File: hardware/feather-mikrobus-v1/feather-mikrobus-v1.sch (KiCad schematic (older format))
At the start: 26 parts, among them J1 Adafruit_Feather_socket_heade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, J2 Adafruit_Feather_socket_heade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, J3 mikroBUS_socket_header_left_p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, J4 mikroBUS_socket_header_right_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, SW1 JS102011SAQN, SW2 KMR421GULCLFS, SW3 KMR421GULCLFS

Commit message: Update symbols and minor cleanup
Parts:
- removed A1: Adafruit_Feather_socket_empty, Flying_Camp_Design:Adafruit_Feather_socket_empty, symbol Flying_Camp_Design:Adafruit_Feather_socket_empty
- removed A2: mikroBUS_socket_empty, Flying_Camp_Design:mikroBUS_socket_empty, symbol Flying_Camp_Design:mikroBUS_socket_empty
- C1: value GRM188R72A104KA35D -> Murata_GRM188R72A104KA35D; symbol Flying_Camp_Design:GRM188R72A104KA35D -> Flying_Camp_Design:Murata_GRM188R72A104KA35D
- D1, D2: value LTST-C191KGKT -> Lite-On_LTST-C191KGKT; symbol Flying_Camp_Design:LTST-C191KGKT -> Flying_Camp_Design:Lite-On_LTST-C191KGKT
- LOGO1: value mikroBUS_logo -> mikroBUS-Logo_11.9x4.1mm_SilkScreen; symbol Flying_Camp_Design:mikroBUS_logo -> Flying_Camp_Design:mikroBUS-Logo_11.9x4.1mm_SilkScreen
- LOGO3: value Adafruit_Feather_logo -> Adafruit_Feather_logo_13.87x6.33mm_silkscreen; footprint Flying_Camp_Design:Adafruit_Feather_logo -> Flying_Camp_Design:Adafruit_Feather_logo_13.87x6.33mm_silkscreen; symbol Flying_Camp_Design:Adafruit_Feather_logo -> Flying_Camp_Design:Adafruit_Feather_logo_13.87x6.33mm_silkscreen
- R1: value RC0603JR-071KL -> Yageo_RC0603JR-071KL; symbol Flying_Camp_Design:RC0603JR-071KL -> Flying_Camp_Design:Yageo_RC0603JR-071KL
- R2, R8: value RC0603JR-07330RL -> Yageo_RC0603JR-07330RL; symbol Flying_Camp_Design:RC0603JR-07330RL -> Flying_Camp_Design:Yageo_RC0603JR-07330RL
- R3, R4: value RC0603JR-074K7L -> Yageo_RC0603JR-074K7L; symbol Flying_Camp_Design:RC0603JR-074K7L -> Flying_Camp_Design:Yageo_RC0603JR-074K7L; DNP (none) -> DNP
- R5: value RC0603JR-070RL -> Yageo_RC0603JR-070RL; symbol Flying_Camp_Design:RC0603JR-070RL -> Flying_Camp_Design:Yageo_RC0603JR-070RL
- R6: value RC0603JR-0710KL -> Yageo_RC0603JR-0710KL; symbol Flying_Camp_Design:RC0603JR-0710KL -> Flying_Camp_Design:Yageo_RC0603JR-0710KL
- R7: value RC0603JR-07100RL -> Yageo_RC0603JR-07100RL; symbol Flying_Camp_Design:RC0603JR-07100RL -> Flying_Camp_Design:Yageo_RC0603JR-07100RL
- SW1: value JS102011SAQN -> C_and_K_JS102011SAQN; footprint Flying_Camp_Design:JS102011SAQN -> Flying_Camp_Design:C_and_K_JS102011SAQN; symbol Flying_Camp_Design:JS102011SAQN -> Flying_Camp_Design:C_and_K_JS102011SAQN
- SW2, SW3: value KMR421GULCLFS -> C_and_K_KMR421GULCLFS; footprint Flying_Camp_Design:KMR421GULCLFS -> Flying_Camp_Design:C_and_K_KMR421GULCLFS; symbol Flying_Camp_Design:KMR421GULCLFS -> Flying_Camp_Design:C_and_K_KMR421GULCLFS
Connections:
- net labels added: 3V3_LED_R, EN_SW_R, SW2_R, USER_LED_R, ~USER_SW
- net labels removed: USER_SW
- wire segments 106 -> 107
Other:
- note added: "Adafruit STM32F405 Feather Express Notes:\n- No PWM output on D6-D8\n- DAC output available on A0-A1\n- D8 is connected to onboard LED"
- note removed: "Adafruit STM32F405 Feather Express Notes:\n- No PWM output on D6-D8\n- DAC output on A0-A1\n- D8 is connected to onboard LED"
- moved on the sheet: FID1, FID2, FID3, J1, J2, J3, J4

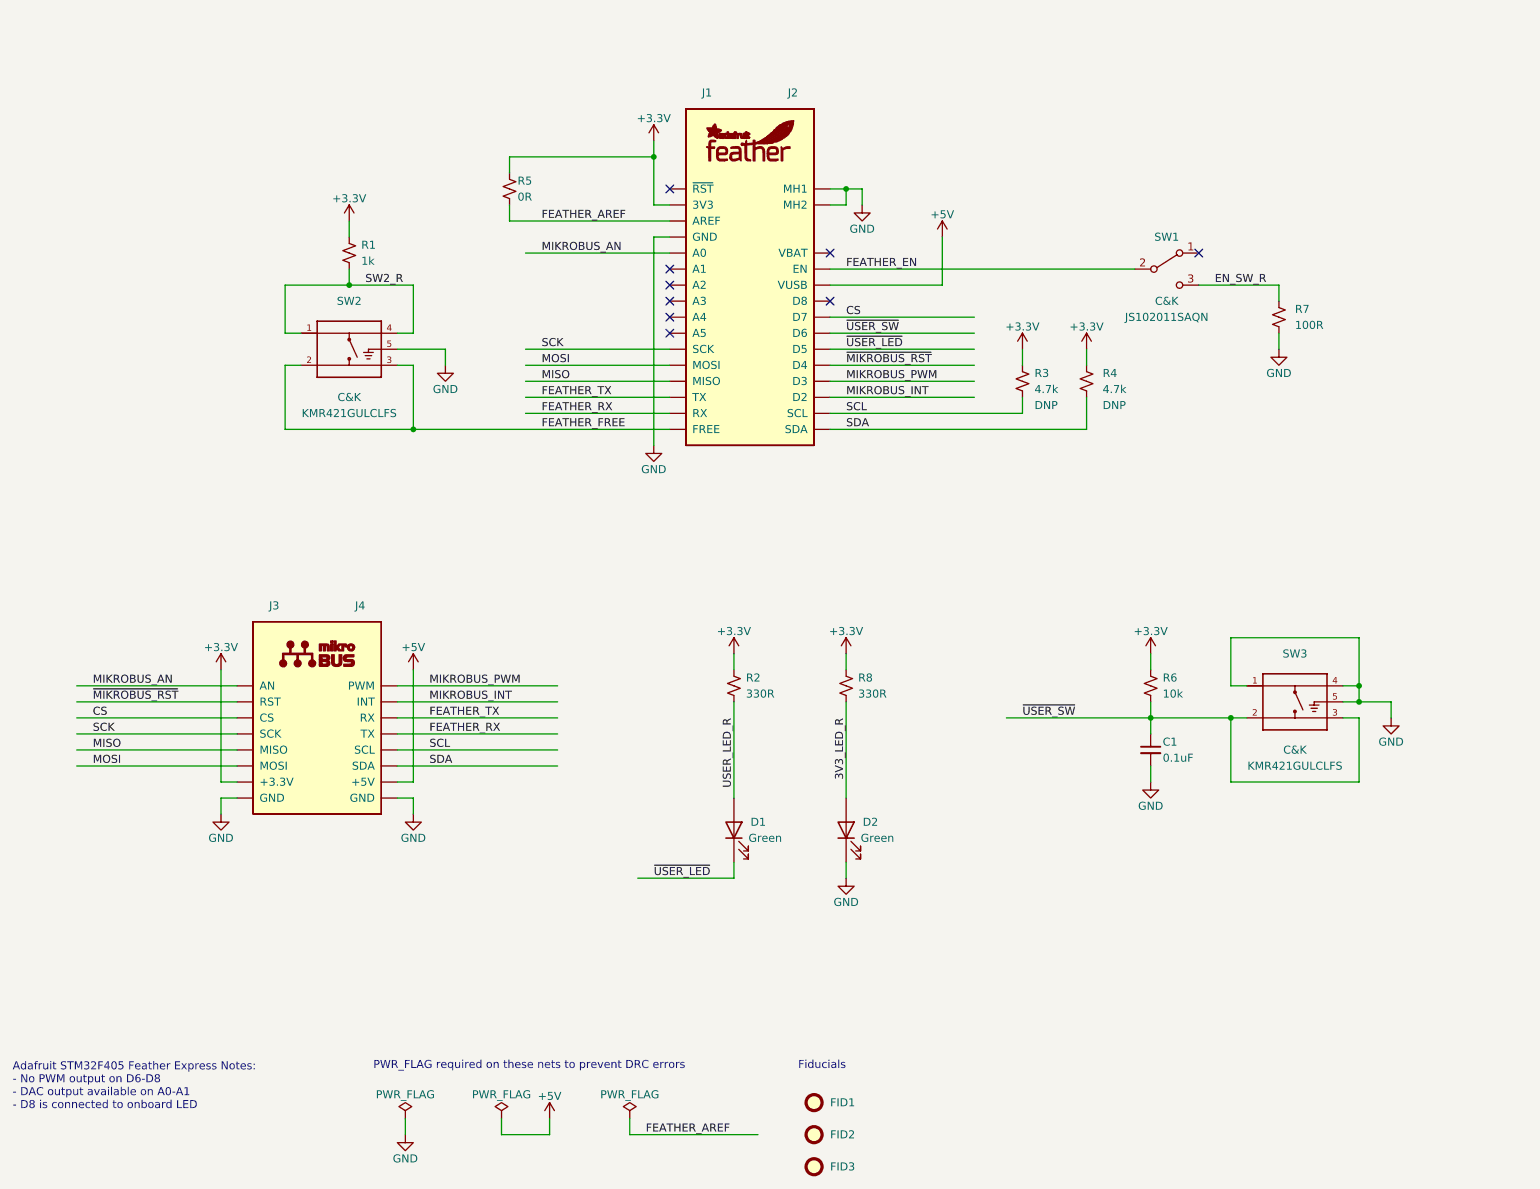
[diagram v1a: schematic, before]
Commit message: Update schematic with finalized manufacturers and vendors
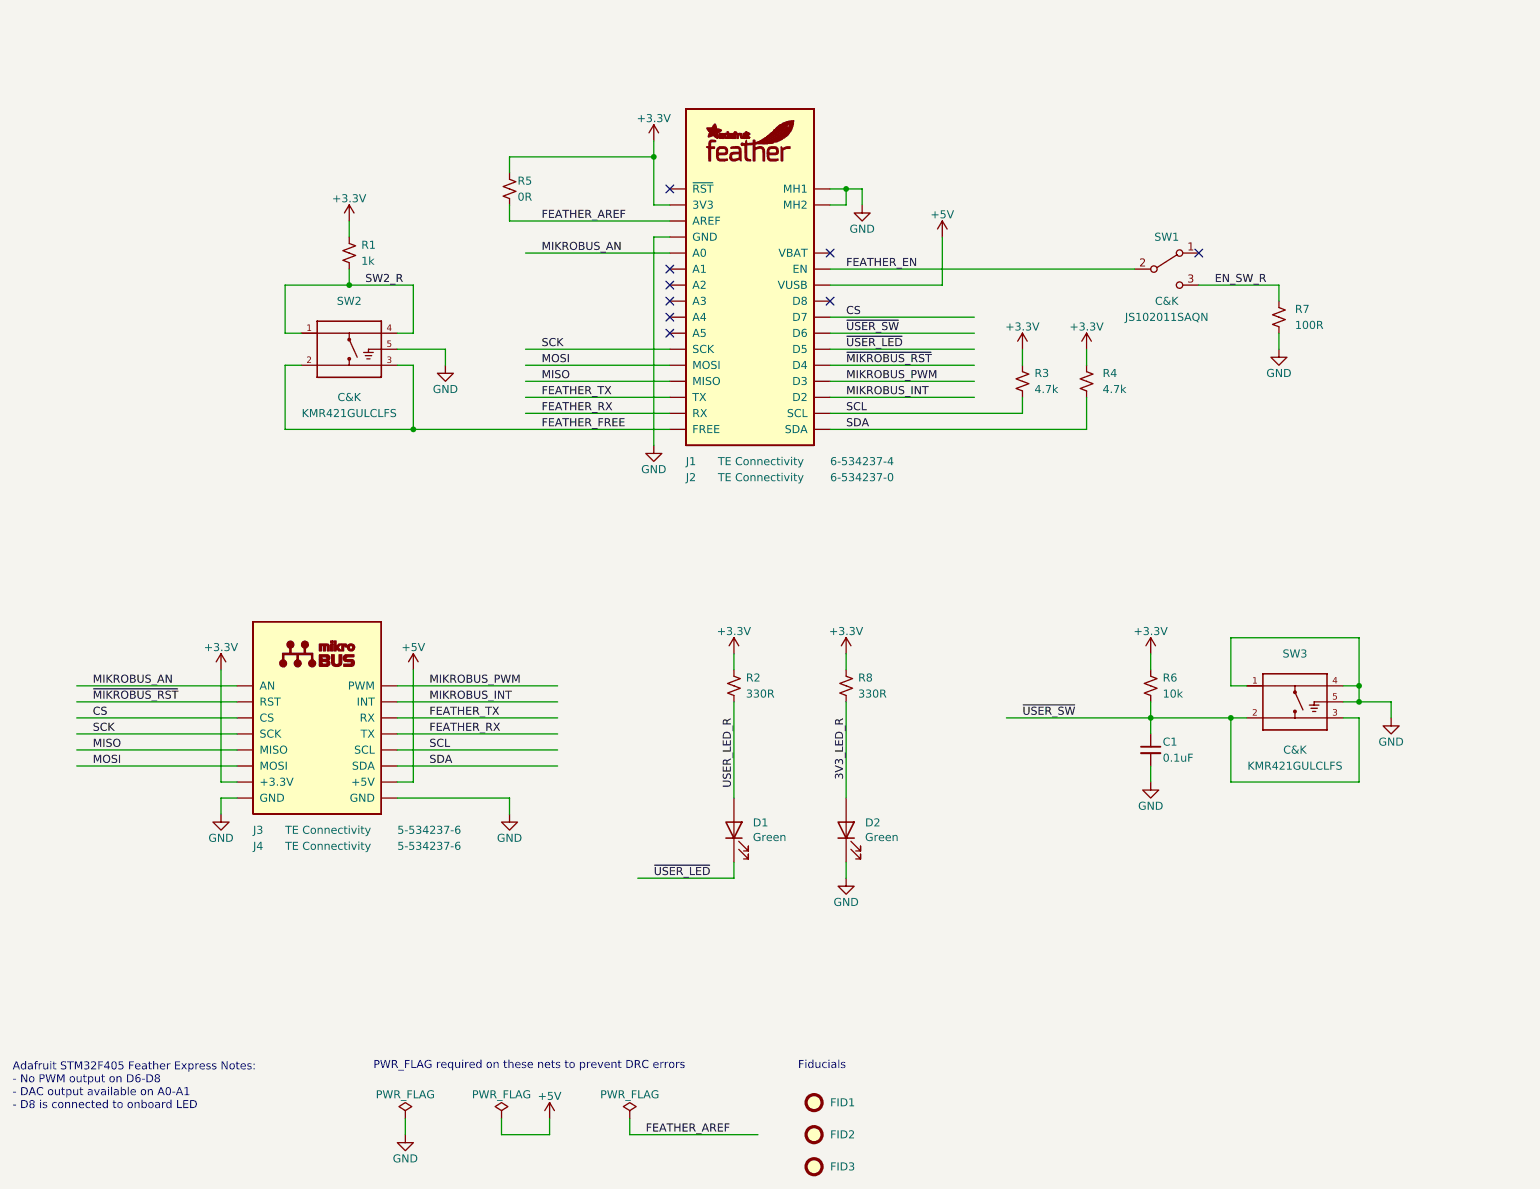
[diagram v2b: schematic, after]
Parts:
- removed D1, D2: Lite-On_LTST-C191KGKT, Flying_Camp_Design:LED_0603_1608Metric, symbol Flying_Camp_Design:Lite-On_LTST-C191KGKT
- added D1, D2: Lite-On_LTST-C193KGKT-5A, Flying_Camp_Design:LED_0603_1608Metric, symbol Flying_Camp_Design:Lite-On_LTST-C193KGKT-5A
- J1: Manufacturer (none) -> TE Connectivity; Manufacturer Part Number (none) -> 6-534237-4; Vendor (none) -> Digi-Key; Vendor Part Number (none) -> A32549-ND; Vendor URL (none) -> https://www.digikey.com/short/z8mb48
- J2: Manufacturer (none) -> TE Connectivity; Manufacturer Part Number (none) -> 6-534237-0; Vendor (none) -> Digi-Key; Vendor Part Number (none) -> A32911-ND; Vendor URL (none) -> https://www.digikey.com/short/z8mbmc
- J3, J4: Manufacturer (none) -> TE Connectivity; Manufacturer Part Number (none) -> 5-534237-6; Vendor (none) -> Digi-Key; Vendor Part Number (none) -> A32909-ND; Vendor URL (none) -> https://www.digikey.com/short/z8mbmb
- R3, R4: DNP DNP -> (none)
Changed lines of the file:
@@
 CS
 Wire Wire Line
-	3300 5400 3300 5500
-Wire Wire Line
-	3200 5400 3300 5400
+	3900 5400 3900 5500
+Wire Wire Line
+	3200 5400 3900 5400
 Wire Wire Line
 	2200 4700 1200 4700
@@
 F 8 "https://www.digikey.com/short/z3bjcp" H 7600 1900 50  0001 L CNN "Vendor URL"
 F 9 "4.7k" H 7600 2750 50  0000 L CNN "Resistance"
-F 10 "DNP" H 7600 2650 50  0000 L CNN "DNP"
 	1    7500 2800
 	1    0    0    -1
@@
 F 8 "https://www.digikey.com/short/z3bjcp" H 7200 1900 50  0001 L CNN "Vendor URL"
 F 9 "4.7k" H 7175 2750 50  0000 L CNN "Resistance"
-F 10 "DNP" H 7175 2650 50  0000 L CNN "DNP"
 	1    7100 2800
 	1    0    0    -1
@@
 U 1 1 5E3B727D
 P 5400 2200
-F 0 "J1" H 5100 3400 50  0000 L CNN
+F 0 "J1" H 5000 1100 50  0000 L CNN
 F 1 "Adafruit_Feather_socket_header_left_pth" H 5400 900 50  0001 C CNN
 F 2 "Flying_Camp_Design:Adafruit_Feather_socket_header_left_pth" H 5400 800 50  0001 C CNN
-F 3 "https://learn.adafruit.com/adafruit-feather/feather-specification" H 5400 700 50  0001 C CNN
+F 3 "https://www.te.com/commerce/DocumentDelivery/DDEController?Action=srchrtrv&DocNm=534237&DocType=Customer+Drawing&DocLang=English" H 5400 700 50  0001 C CNN
+F 4 "TE Connectivity" H 5200 1100 50  0000 L CNN "Manufacturer"
+F 5 "6-534237-4" H 5900 1100 50  0000 L CNN "Manufacturer Part Number"
+F 6 "Digi-Key" H 0   0   50  0001 C CNN "Vendor"
+F 7 "A32549-ND" H 0   0   50  0001 C CNN "Vendor Part Number"
+F 8 "https://www.digikey.com/short/z8mb48" H 0   0   50  0001 C CNN "Vendor URL"
 	1    5400 2200
 	1    0    0    -1
@@
 U 1 1 5E3B67CD
 P 5400 2200
-F 0 "J2" H 5700 3400 50  0000 R CNN
+F 0 "J2" H 5000 1000 50  0000 L CNN
 F 1 "Adafruit_Feather_socket_header_right_pth" H 5400 900 50  0001 C CNN
 F 2 "Flying_Camp_Design:Adafruit_Feather_socket_header_right_pth" H 5400 800 50  0001 C CNN
-F 3 "https://learn.adafruit.com/adafruit-feather/feather-specification" H 5400 700 50  0001 C CNN
+F 3 "https://www.te.com/commerce/DocumentDelivery/DDEController?Action=srchrtrv&DocNm=534237&DocType=Customer+Drawing&DocLang=English" H 5400 700 50  0001 C CNN
+F 4 "TE Connectivity" H 5200 1000 50  0000 L CNN "Manufacturer"
+F 5 "6-534237-0" H 5900 1000 50  0000 L CNN "Manufacturer Part Number"
+F 6 "Digi-Key" H 0   0   50  0001 C CNN "Vendor"
+F 7 "A32911-ND" H 0   0   50  0001 C CNN "Vendor Part Number"
+F 8 "https://www.digikey.com/short/z8mbmc" H 0   0   50  0001 C CNN "Vendor URL"
 	1    5400 2200
 	1    0    0    -1
@@
 L Flying_Camp_Design:GND #PWR012
 U 1 1 5E3D743E
-P 3300 5500
-F 0 "#PWR012" H 3300 5250 50  0001 C CNN
-F 1 "GND" H 3300 5350 50  0000 C CNN
-F 2 "" H 3300 5500 50  0001 C CNN
-F 3 "" H 3300 5500 50  0001 C CNN
-	1    3300 5500
+P 3900 5500
+F 0 "#PWR012" H 3900 5250 50  0001 C CNN
+F 1 "GND" H 3900 5350 50  0000 C CNN
+F 2 "" H 3900 5500 50  0001 C CNN
+F 3 "" H 3900 5500 50  0001 C CNN
+	1    3900 5500
 	1    0    0    -1
 $EndComp
@@
 U 1 1 5E3C6EE3
 P 2700 4900
-F 0 "J3" H 2400 5600 50  0000 L CNN
+F 0 "J3" H 2300 4200 50  0000 L CNN
 F 1 "mikroBUS_socket_header_left_pth" H 2700 4000 50  0001 C CNN
 F 2 "Flying_Camp_Design:mikroBUS_socket_header_left_pth" H 2700 3900 50  0001 C CNN
-F 3 "https://www.mikroe.com/mikrobus" H 2700 3800 50  0001 C CNN
+F 3 "https://www.te.com/commerce/DocumentDelivery/DDEController?Action=srchrtrv&DocNm=534237&DocType=Customer+Drawing&DocLang=English" H 2700 3800 50  0001 C CNN
+F 4 "TE Connectivity" H 2500 4200 50  0000 L CNN "Manufacturer"
+F 5 "5-534237-6" H 3200 4200 50  0000 L CNN "Manufacturer Part Number"
+F 6 "Digi-Key" H 0   0   50  0001 C CNN "Vendor"
+F 7 "A32909-ND" H 0   0   50  0001 C CNN "Vendor Part Number"
+F 8 "https://www.digikey.com/short/z8mbmb" H 0   0   50  0001 C CNN "Vendor URL"
 	1    2700 4900
 	1    0    0    -1
@@
 U 1 1 5E3C7996
 P 2700 4900
-F 0 "J4" H 3000 5600 50  0000 R CNN
+F 0 "J4" H 2300 4100 50  0000 L CNN
 F 1 "mikroBUS_socket_header_right_pth" H 2700 4000 50  0001 C CNN
 F 2 "Flying_Camp_Design:mikroBUS_socket_header_right_pth" H 2700 3900 50  0001 C CNN
-F 3 "https://www.mikroe.com/mikrobus" H 2700 3800 50  0001 C CNN
+F 3 "https://www.te.com/commerce/DocumentDelivery/DDEController?Action=srchrtrv&DocNm=534237&DocType=Customer+Drawing&DocLang=English" H 2700 3800 50  0001 C CNN
+F 4 "TE Connectivity" H 2500 4100 50  0000 L CNN "Manufacturer"
+F 5 "5-534237-6" H 3200 4100 50  0000 L CNN "Manufacturer Part Number"
+F 6 "Digi-Key" H 0   0   50  0001 C CNN "Vendor"
+F 7 "A32909-ND" H 0   0   50  0001 C CNN "Vendor Part Number"
+F 8 "https://www.digikey.com/short/z8mbmb" H 0   0   50  0001 C CNN "Vendor URL"
 	1    2700 4900
 	1    0    0    -1
@@
 $EndComp
 $Comp
-L Flying_Camp_Design:Lite-On_LTST-C191KGKT D1
-U 1 1 5E653E2F
+L Flying_Camp_Design:Lite-On_LTST-C193KGKT-5A D1
+U 1 1 5E68E113
 P 5300 5600
-F 0 "D1" V 5350 5400 50  0000 L CNN
-F 1 "Lite-On_LTST-C191KGKT" H 5300 5300 50  0001 C CNN
+F 0 "D1" V 5346 5482 50  0000 R CNN
+F 1 "Lite-On_LTST-C193KGKT-5A" H 5300 5300 50  0001 C CNN
 F 2 "Flying_Camp_Design:LED_0603_1608Metric" H 5300 5200 50  0001 C CNN
-F 3 "http://optoelectronics.liteon.com/upload/download/DS22-2000-228/LTST-C191KGKT.PDF" H 5300 5100 50  0001 C CNN
+F 3 "http://optoelectronics.liteon.com/upload/download/DS22-2007-0094/LTST-C193KGKT-5A.PDF" H 5300 5100 50  0001 C CNN
 F 4 "Lite-On Inc." H 5300 5000 50  0001 C CNN "Manufacturer"
-F 5 "LTST-C191KGKT" H 5300 4900 50  0001 C CNN "Manufacturer Part Number"
+F 5 "LTST-C193KGKT-5A" H 5300 4900 50  0001 C CNN "Manufacturer Part Number"
 F 6 "Digi-Key" H 5300 4800 50  0001 C CNN "Vendor"
-F 7 "160-1446-1-ND" H 5300 4700 50  0001 C CNN "Vendor Part Number"
-F 8 "https://www.digikey.com/short/z35jf3" H 5300 4600 50  0001 C CNN "Vendor URL"
-F 9 "Green" V 5250 5300 50  0000 L CNN "Color"
+F 7 "160-1828-1-ND" H 5300 4700 50  0001 C CNN "Vendor Part Number"
+F 8 "https://www.digikey.com/short/z8m54d" H 5300 4600 50  0001 C CNN "Vendor URL"
+F 9 "Green" V 5255 5482 50  0000 R CNN "Color"
 	1    5300 5600
 	0    -1   -1   0
 $EndComp
 $Comp
-L Flying_Camp_Design:Lite-On_LTST-C191KGKT D2
-U 1 1 5E49AFFA
+L Flying_Camp_Design:Lite-On_LTST-C193KGKT-5A D2
+U 1 1 5E68EC6D
 P 6000 5600
-F 0 "D2" V 6050 5400 50  0000 L CNN
-F 1 "Lite-On_LTST-C191KGKT" H 6000 5300 50  0001 C CNN
+F 0 "D2" V 6046 5482 50  0000 R CNN
+F 1 "Lite-On_LTST-C193KGKT-5A" H 6000 5300 50  0001 C CNN
 F 2 "Flying_Camp_Design:LED_0603_1608Metric" H 6000 5200 50  0001 C CNN
-F 3 "http://optoelectronics.liteon.com/upload/download/DS22-2000-228/LTST-C191KGKT.PDF" H 6000 5100 50  0001 C CNN
+F 3 "http://optoelectronics.liteon.com/upload/download/DS22-2007-0094/LTST-C193KGKT-5A.PDF" H 6000 5100 50  0001 C CNN
 F 4 "Lite-On Inc." H 6000 5000 50  0001 C CNN "Manufacturer"
-F 5 "LTST-C191KGKT" H 6000 4900 50  0001 C CNN "Manufacturer Part Number"
+F 5 "LTST-C193KGKT-5A" H 6000 4900 50  0001 C CNN "Manufacturer Part Number"
 F 6 "Digi-Key" H 6000 4800 50  0001 C CNN "Vendor"
-F 7 "160-1446-1-ND" H 6000 4700 50  0001 C CNN "Vendor Part Number"
-F 8 "https://www.digikey.com/short/z35jf3" H 6000 4600 50  0001 C CNN "Vendor URL"
-F 9 "Green" V 5950 5300 50  0000 L CNN "Color"
+F 7 "160-1828-1-ND" H 6000 4700 50  0001 C CNN "Vendor Part Number"
+F 8 "https://www.digikey.com/short/z8m54d" H 6000 4600 50  0001 C CNN "Vendor URL"
+F 9 "Green" V 5955 5482 50  0000 R CNN "Color"
 	1    6000 5600
 	0    -1   -1   0
